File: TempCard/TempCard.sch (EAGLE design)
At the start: 13 parts, among them Q1 MOSFET-NCHANNELBSS138, Q2 MOSFET-NCHANNELBSS138, U1 MIC5219 3.3V

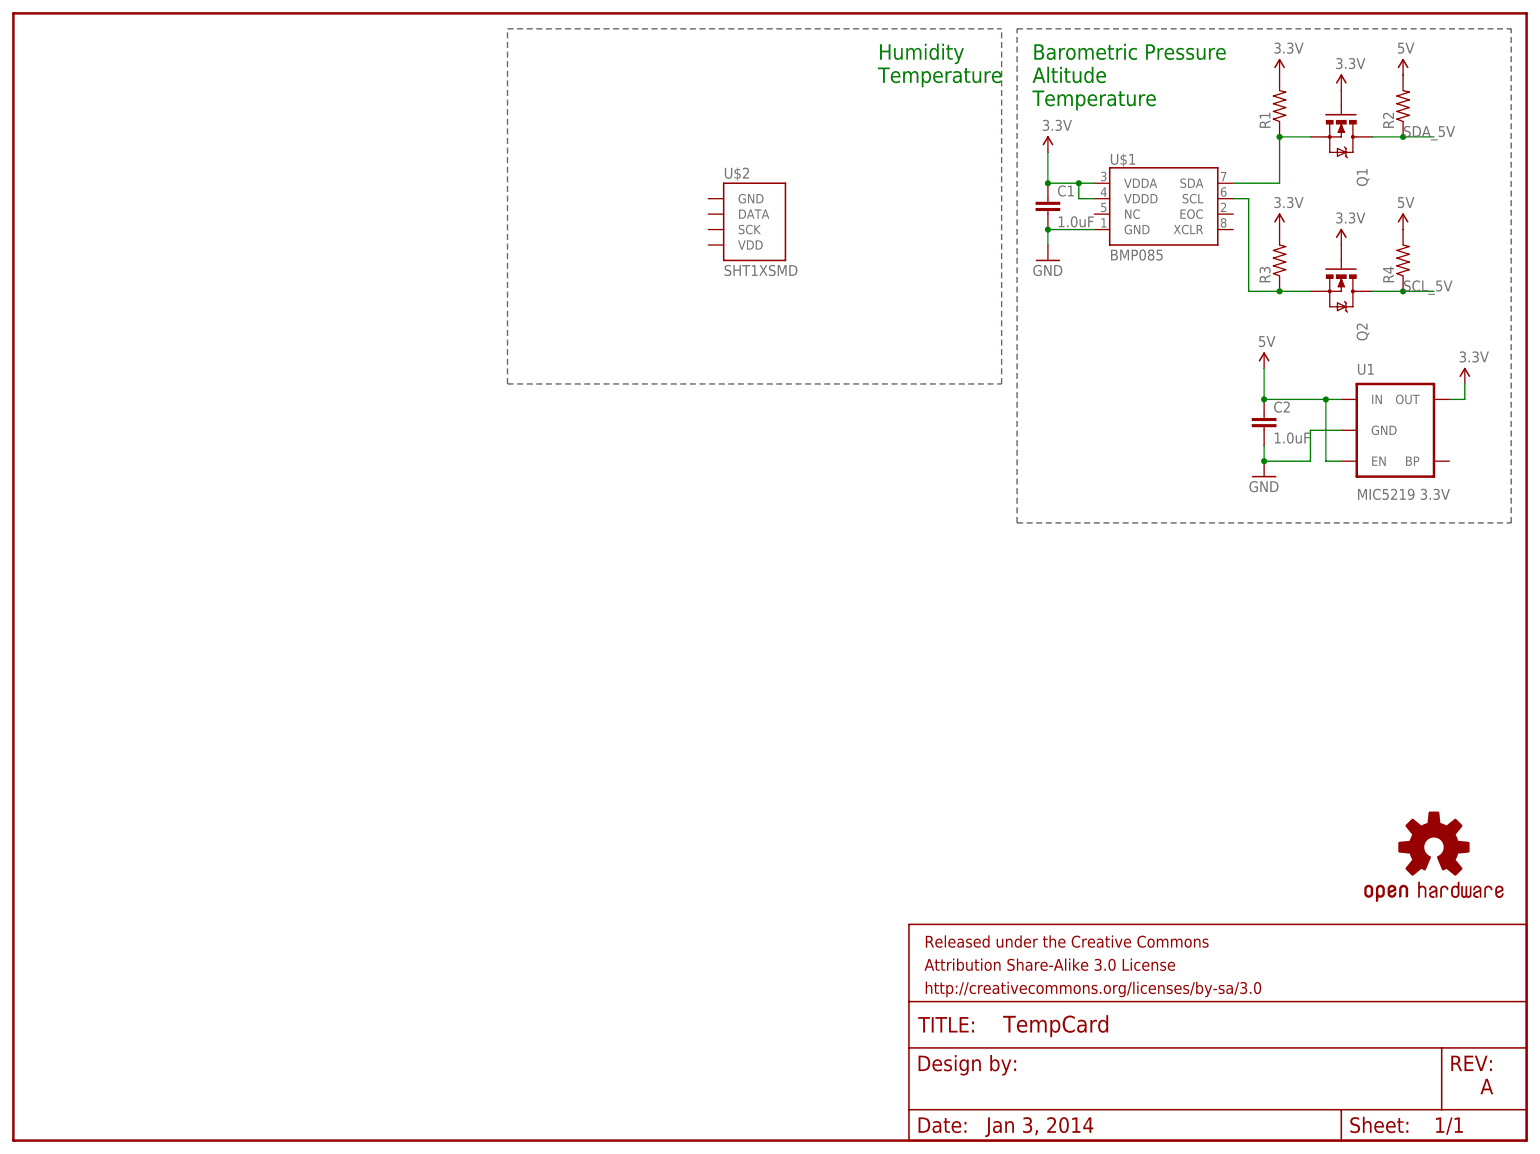
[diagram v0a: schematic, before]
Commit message: Adding sensors
BMP085, HMC5883L, SHT15

Signed-off-by: Scott Lerner <scottphiliplerner@gmail.com>
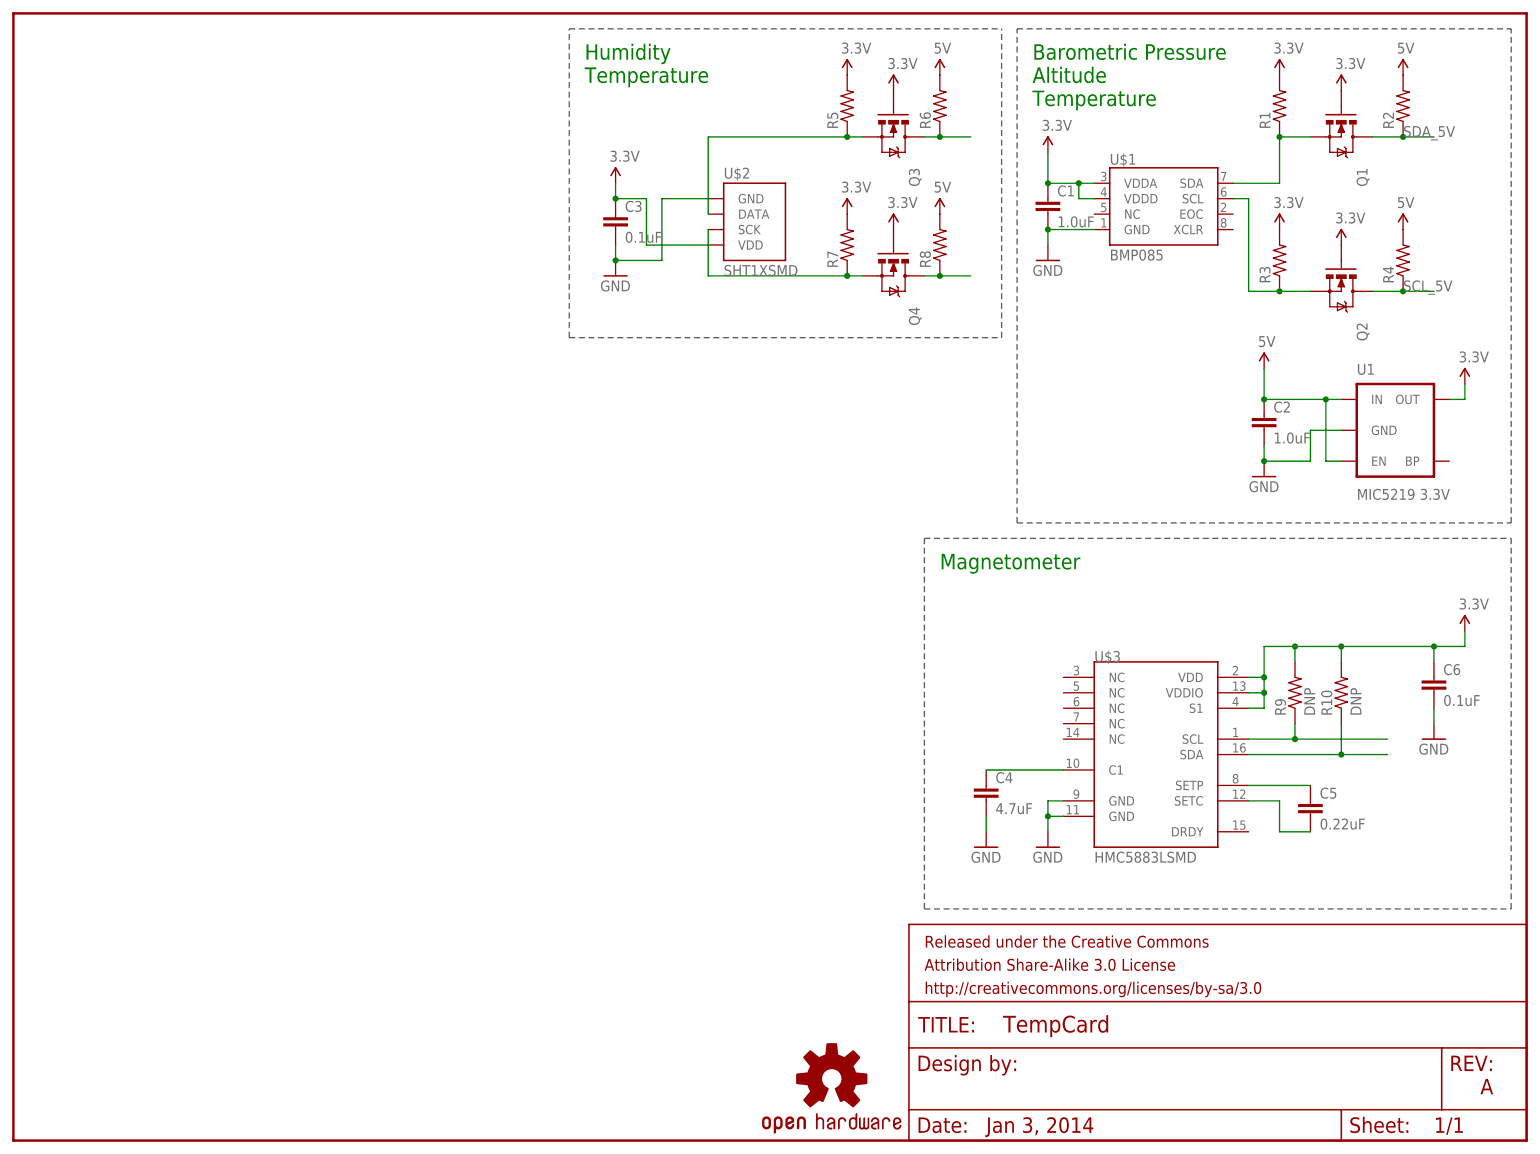
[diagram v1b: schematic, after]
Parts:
- added C3: 0.1uF, SparkFun-Capacitors:1.0UF-25V-+80/-20(0805)
- added C4: 4.7uF, SparkFun-Passives:CAP0402-CAP
- added C5: 0.22uF, SparkFun-Passives:CAP0402-CAP
- added C6: 0.1uF, SparkFun-Passives:CAP0402-CAP
- added Q3, Q4: MOSFET-NCHANNELBSS138, SparkFun-DiscreteSemi:MOSFET-NCHANNELBSS138
- added R10, R9: DNP, SparkFun-Passives:RESISTOR0402-RES
- added R5, R6, R7, R8: (no value), SparkFun-Resistors:RESISTOR0805-RES
- added U$3: HMC5883LSMD, SparkFun-Sensors:HMC5883LSMD
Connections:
- new net N$10: R9.1, U$3.SCL
- new net N$11: R10.1, U$3.SDA
- new net N$3: C4.1, U$3.C1
- new net N$4: Q3.D, R6.1
- new net N$5: Q4.S, R7.1, U$2.SCK
- new net N$6: Q4.D, R8.1
- new net N$7: C5.1, U$3.SETP
- new net N$8: C5.2, U$3.SETC
- new net N$9: Q3.S, R5.1, U$2.DATA
- net 3.3V: now also C3.1, C6.1, Q3.G, Q4.G, R10.2, R5.2, R7.2, R9.2, U$2.VDD, U$3.S1, U$3.VDD, U$3.VDDIO
- net 5V: now also R6.2, R8.2
- net GND: now also C3.2, C4.2, C6.2, U$2.GND, U$3.GND@1, U$3.GND@2
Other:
- note added: "Magnetometer"

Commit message: MCU/Sensor Edit
Switched the magnetometer. Added potential MCUs for Atmel and PIC. More than likely going with ATTiny85. More testing to follow.

Signed-off-by: Scott Lerner <scottphiliplerner@gmail.com>
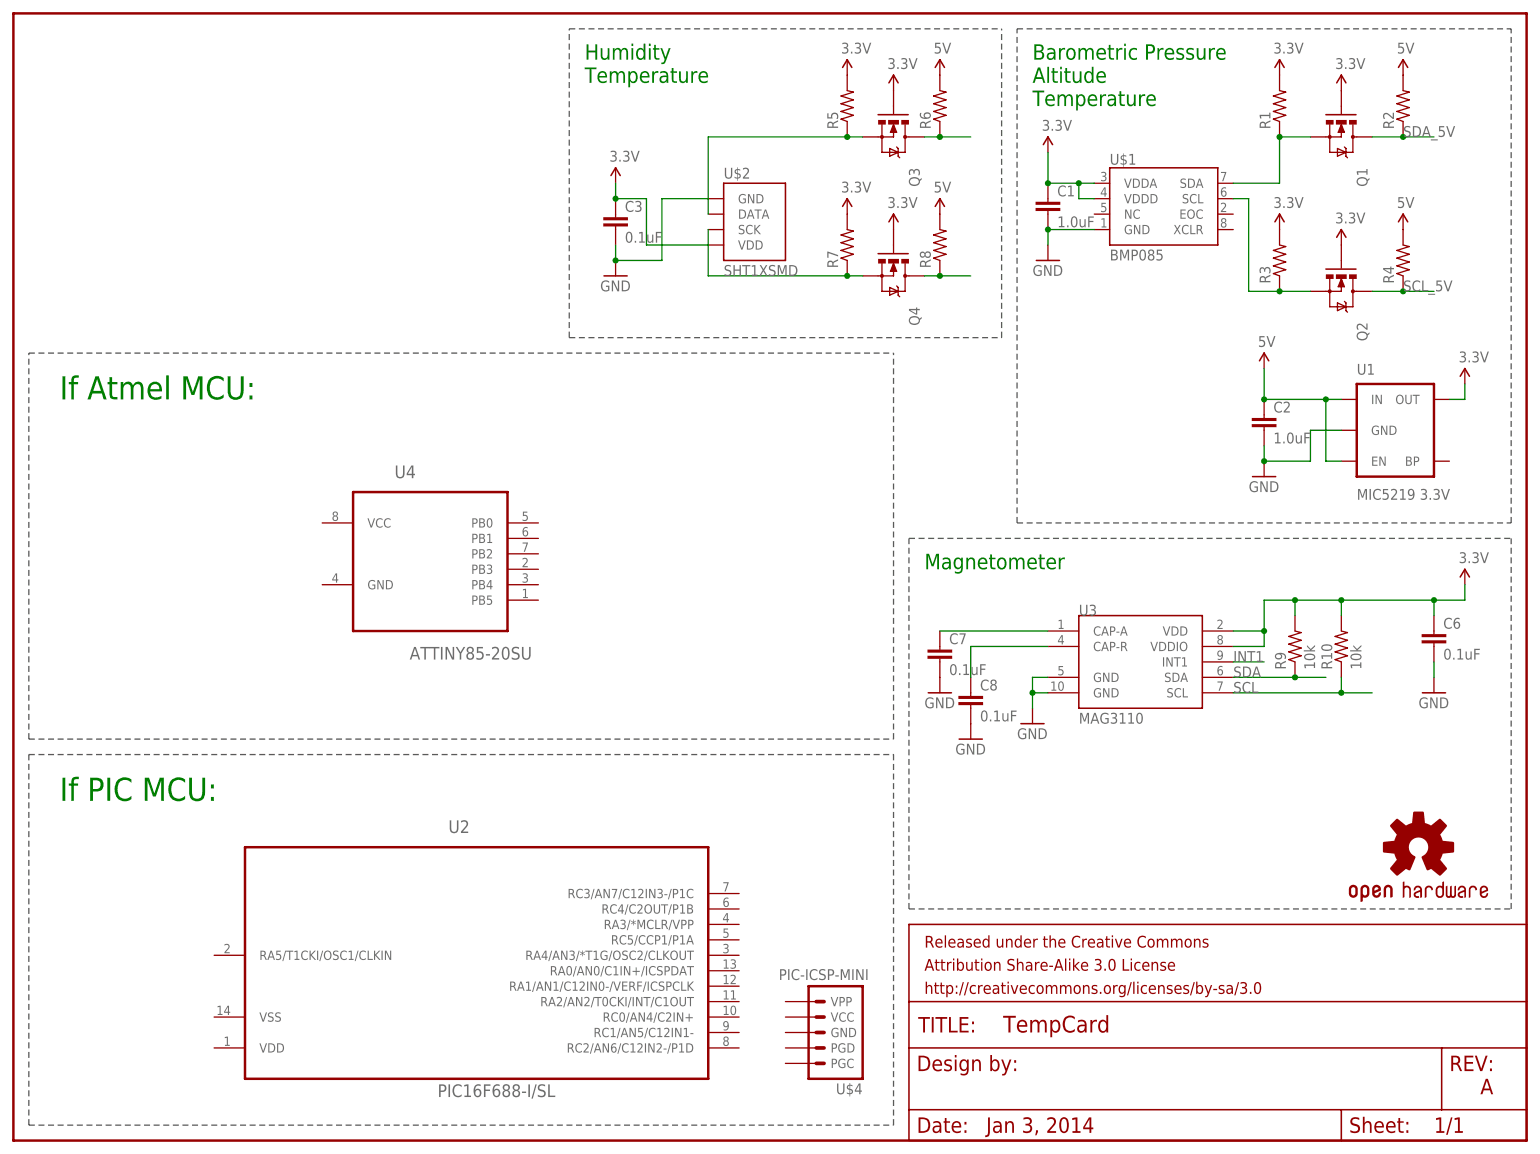
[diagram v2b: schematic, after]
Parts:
- removed C4: 4.7uF, SparkFun-Passives:CAP0402-CAP
- removed C5: 0.22uF, SparkFun-Passives:CAP0402-CAP
- removed U$3: HMC5883LSMD, SparkFun-Sensors:HMC5883LSMD
- added C7, C8: 0.1uF, SparkFun-Passives:CAP0402-CAP
- added U$4: PIC-ICSP-MINI, SparkFun-Connectors:PIC-ICSP-MINI
- added U2: PIC16F688-I/SL, Microchip_By_element14_Batch_1:PIC16F688-I/SL
- added U3: MAG3110, SparkFun-Sensors:MAG3110
- added U4: ATTINY85-20SU, Atmel_By_element14_Batch_1:ATTINY85-20SU
- R10, R9: value DNP -> 10k
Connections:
- removed net N$10: R9.1, U$3.SCL
- removed net N$11: R10.1, U$3.SDA
- removed net N$3: C4.1, U$3.C1
- removed net N$7: C5.1, U$3.SETP
- removed net N$8: C5.2, U$3.SETC
- new net INT1: U3.INT1
- new net N$12: C7.1, U3.CAP-A
- new net N$13: C8.1, U3.CAP-R
- new net SCL: R10.1, U3.SCL
- new net SDA: R9.1, U3.SDA
- net 3.3V: now also U3.VDD, U3.VDDIO; no longer U$3.S1, U$3.VDD, U$3.VDDIO
- net GND: now also C7.2, C8.2, U3.GND@10, U3.GND@5; no longer C4.2, U$3.GND@1, U$3.GND@2
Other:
- note added: "If Atmel MCU:"
- note added: "If PIC MCU:"
- moved on the sheet: C6, R10, R9

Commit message: Plane Stuff
I don't know what exactly this changed.

Signed-off-by: Scott Lerner <scottphiliplerner@gmail.com>
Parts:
- removed R10, R9: 10k, SparkFun-Passives:RESISTOR0402-RES
- removed U$4: PIC-ICSP-MINI, SparkFun-Connectors:PIC-ICSP-MINI
- removed U2: PIC16F688-I/SL, Microchip_By_element14_Batch_1:PIC16F688-I/SL
- added C4: 0.1uF, SparkFun-Capacitors:1.0UF-25V-+80/-20(0805)
- added R11, R12: 10k, SparkFun-Resistors:RESISTOR0805-RES
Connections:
- removed net N$4: Q3.D, R6.1
- removed net N$6: Q4.D, R8.1
- removed net SCL_5V: Q2.D, R4.1
- removed net SDA_5V: Q1.D, R2.1
- net 3.3V: no longer R10.2, R9.2
- net 5V: now also C4.1, R11.2, R12.2, U4.VCC
- net GND: now also C4.2, U4.GND
- net SCL: now also Q2.D, Q4.D, R12.1, R4.1, R8.1, U4.PB1; no longer R10.1
- net SDA: now also Q1.D, Q3.D, R11.1, R2.1, R6.1, U4.PB0; no longer R9.1
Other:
- note removed: "If PIC MCU:"
